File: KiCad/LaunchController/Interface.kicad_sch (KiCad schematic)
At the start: 157 parts

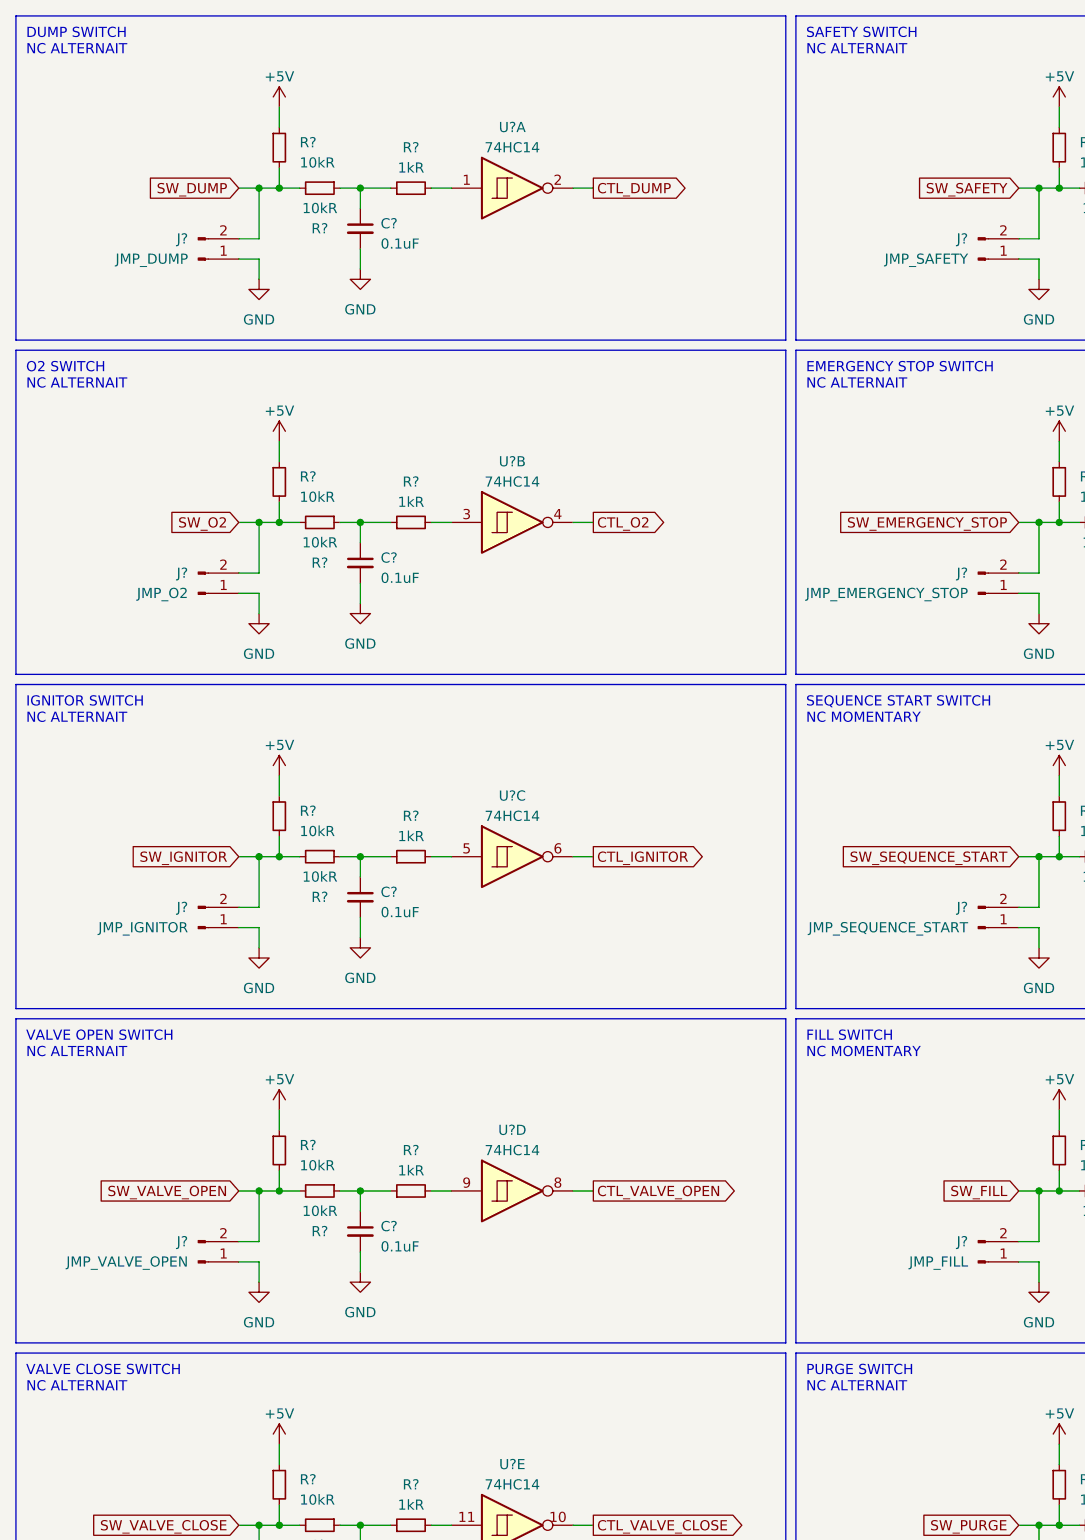
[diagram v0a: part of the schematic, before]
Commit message: スイッチの接点方式を修正
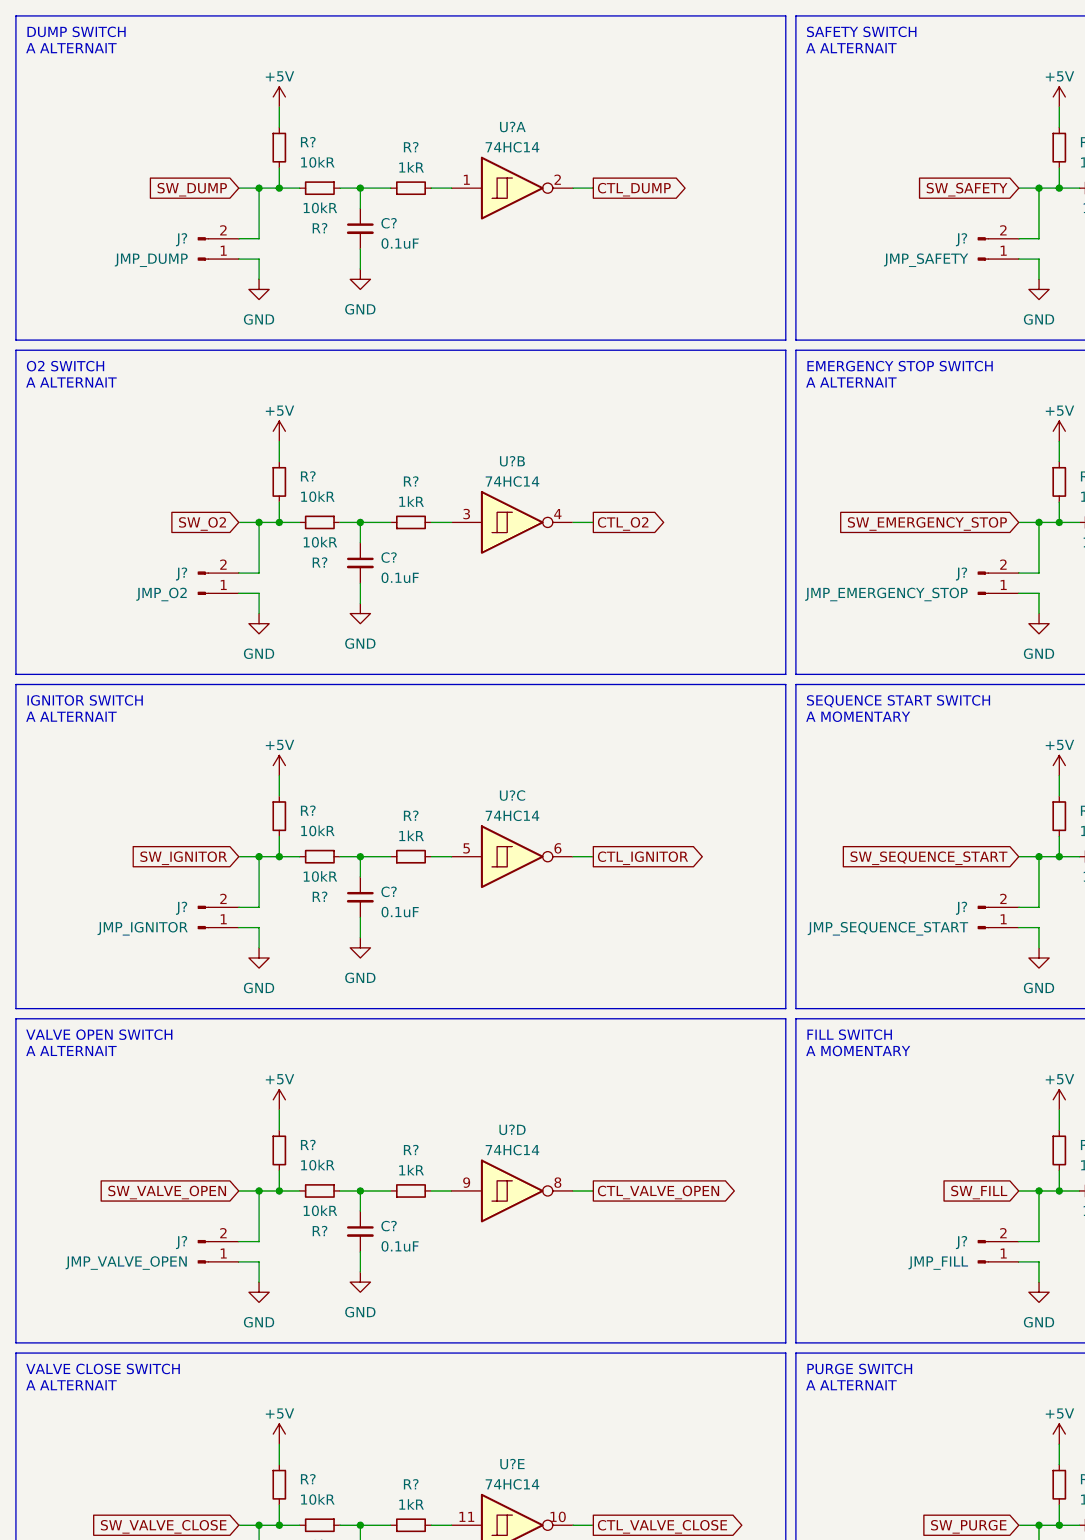
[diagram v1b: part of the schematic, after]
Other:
- note added: "DUMP SWITCH A ALTERNAIT"
- note added: "EMERGENCY STOP SWITCH A ALTERNAIT"
- note added: "FILL SWITCH A MOMENTARY"
- note added: "IGNITOR SWITCH A ALTERNAIT"
- note added: "O2 SWITCH A ALTERNAIT"
- note added: "PURGE SWITCH A ALTERNAIT"
- note added: "SAFETY SWITCH A ALTERNAIT"
- note added: "SEQUENCE START SWITCH A MOMENTARY"
- note added: "VALVE CLOSE SWITCH A ALTERNAIT"
- note added: "VALVE OPEN SWITCH A ALTERNAIT"
- note removed: "DUMP SWITCH NC ALTERNAIT"
- note removed: "EMERGENCY STOP SWITCH NC ALTERNAIT"
- note removed: "FILL SWITCH NC MOMENTARY"
- note removed: "IGNITOR SWITCH NC ALTERNAIT"
- note removed: "O2 SWITCH NC ALTERNAIT"
- note removed: "PURGE SWITCH NC ALTERNAIT"
- note removed: "SAFETY SWITCH NC ALTERNAIT"
- note removed: "SEQUENCE START SWITCH NC MOMENTARY"
- note removed: "VALVE CLOSE SWITCH NC ALTERNAIT"
- note removed: "VALVE OPEN SWITCH NC ALTERNAIT"
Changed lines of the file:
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@@
     (effects (font (size 1.27 1.27)) (justify left bottom))
   )
-  (text "FILL SWITCH\nNC MOMENTARY" (at 111.76 143.51 0)
+  (text "FILL SWITCH\nA MOMENTARY" (at 111.76 143.51 0)
     (effects (font (size 1.27 1.27)) (justify left bottom))
   )
-  (text "EMERGENCY STOP SWITCH\nNC ALTERNAIT" (at 111.76 59.69 0)
+  (text "EMERGENCY STOP SWITCH\nA ALTERNAIT" (at 111.76 59.69 0)
     (effects (font (size 1.27 1.27)) (justify left bottom))
   )
@@
     (effects (font (size 1.27 1.27)) (justify left bottom))
   )
-  (text "IGNITOR SWITCH\nNC ALTERNAIT" (at 13.97 101.6 0)
+  (text "IGNITOR SWITCH\nA ALTERNAIT" (at 13.97 101.6 0)
     (effects (font (size 1.27 1.27)) (justify left bottom))
   )
@@
     (effects (font (size 1.27 1.27)) (justify left bottom))
   )
-  (text "SAFETY SWITCH\nNC ALTERNAIT" (at 111.76 17.78 0)
+  (text "SAFETY SWITCH\nA ALTERNAIT" (at 111.76 17.78 0)
     (effects (font (size 1.27 1.27)) (justify left bottom))
   )
@@
     (effects (font (size 1.27 1.27)) (justify left bottom))
   )
-  (text "O2 SWITCH\nNC ALTERNAIT" (at 13.97 59.69 0)
+  (text "O2 SWITCH\nA ALTERNAIT" (at 13.97 59.69 0)
     (effects (font (size 1.27 1.27)) (justify left bottom))
   )
@@
     (effects (font (size 1.27 1.27)) (justify left bottom))
   )
-  (text "VALVE CLOSE SWITCH\nNC ALTERNAIT" (at 13.97 185.42 0)
+  (text "VALVE CLOSE SWITCH\nA ALTERNAIT" (at 13.97 185.42 0)
     (effects (font (size 1.27 1.27)) (justify left bottom))
   )
@@
     (effects (font (size 1.27 1.27)) (justify left bottom))
   )
-  (text "PURGE SWITCH\nNC ALTERNAIT" (at 111.76 185.42 0)
+  (text "PURGE SWITCH\nA ALTERNAIT" (at 111.76 185.42 0)
     (effects (font (size 1.27 1.27)) (justify left bottom))
   )
-  (text "SEQUENCE START SWITCH\nNC MOMENTARY" (at 111.76 101.6 0)
+  (text "SEQUENCE START SWITCH\nA MOMENTARY" (at 111.76 101.6 0)
     (effects (font (size 1.27 1.27)) (justify left bottom))
   )
-  (text "DUMP SWITCH\nNC ALTERNAIT" (at 13.97 17.78 0)
+  (text "DUMP SWITCH\nA ALTERNAIT" (at 13.97 17.78 0)
     (effects (font (size 1.27 1.27)) (justify left bottom))
   )
-  (text "VALVE OPEN SWITCH\nNC ALTERNAIT" (at 13.97 143.51 0)
+  (text "VALVE OPEN SWITCH\nA ALTERNAIT" (at 13.97 143.51 0)
     (effects (font (size 1.27 1.27)) (justify left bottom))
   )

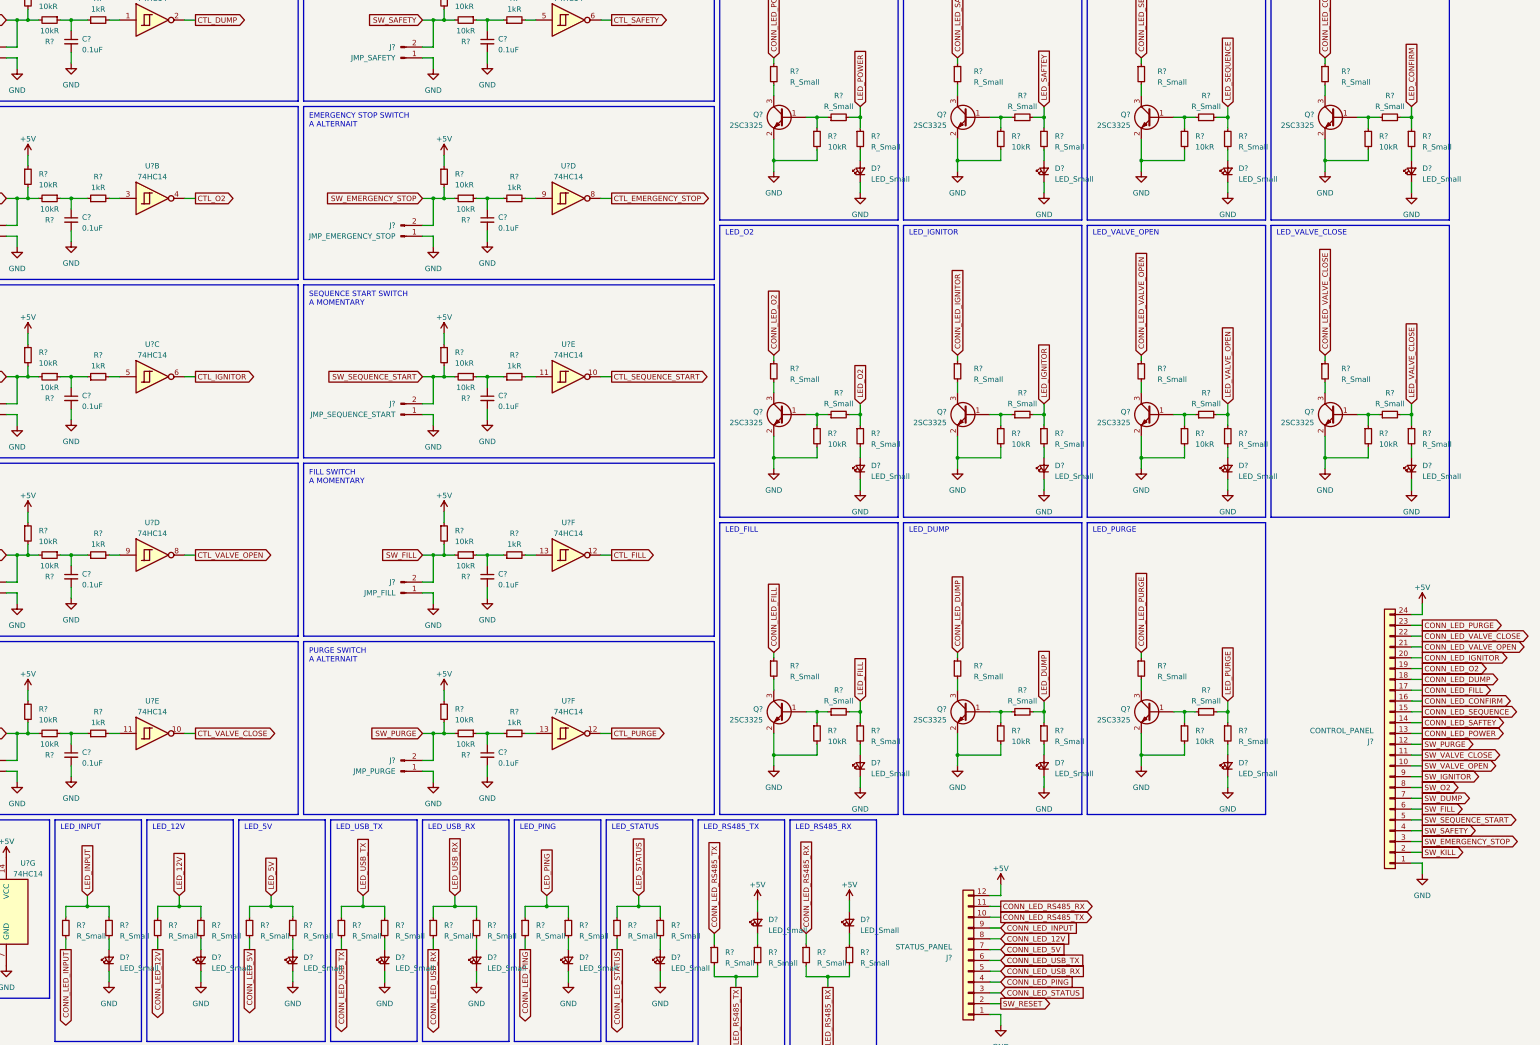
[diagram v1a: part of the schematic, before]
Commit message: LED用の抵抗値を設定
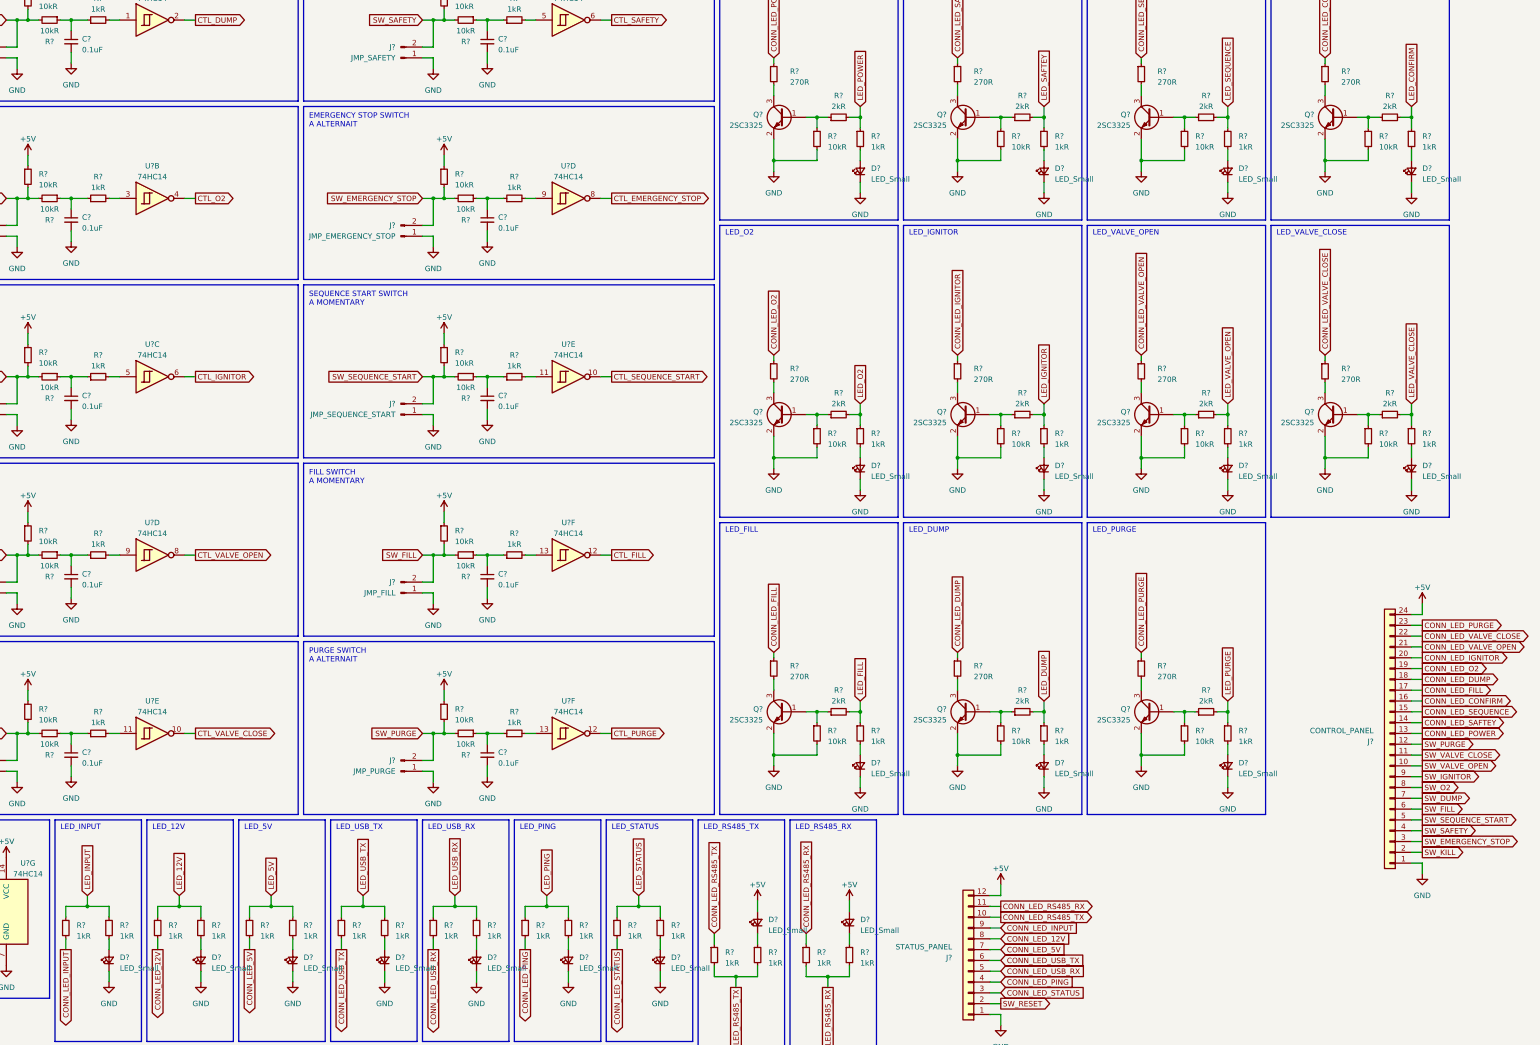
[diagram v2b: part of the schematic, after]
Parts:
- R? (x11): value R_Small -> 270R
- R? (x29): value R_Small -> 1kR
- R? (x11): value R_Small -> 2kR

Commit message: 一通り部品を選定
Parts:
- removed J?: CONTROL_PANEL, symbol Connector_Generic:Conn_01x24
- added J?: INDICATOR_PANEL, Connector_JST:JST_XH_B12B-XH-A_1x12_P2.50mm_Vertical, symbol Connector_Generic:Conn_01x12
- added J?: CONTROL_PANEL, Connector_JST:JST_XH_B12B-XH-A_1x12_P2.50mm_Vertical, symbol Connector_Generic:Conn_01x12
- C? (x10): footprint (none) -> Capacitor_SMD:C_0603_1608Metric_Pad1.08x0.95mm_HandSolder
- D? (x20): value LED_Small -> LED; footprint (none) -> LED_SMD:LED_0603_1608Metric_Pad1.05x0.95mm_HandSolder
- J? (x10): footprint (none) -> Connector_PinHeader_2.54mm:PinHeader_1x02_P2.54mm_Vertical
- J?: footprint (none) -> Connector_JST:JST_XH_B12B-XH-A_1x12_P2.50mm_Vertical
- Q? (x11): value 2SC3325 -> 2SC3325-Y; footprint (none) -> Package_TO_SOT_SMD:SC-59_Handsoldering
- R? (x92): footprint (none) -> Resistor_SMD:R_0603_1608Metric_Pad0.98x0.95mm_HandSolder
- U? (x12): value 74HC14 -> U74HC14; footprint (none) -> Package_DIP:DIP-14_W7.62mm
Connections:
- net +5V: now also J?.12 (Pin_12)
- net CONN_LED_CONFIRM: now also J?.4 (Pin_4)
- net CONN_LED_DUMP: now also J?.6 (Pin_6)
- net CONN_LED_FILL: now also J?.5 (Pin_5)
- net CONN_LED_IGNITOR: now also J?.8 (Pin_8)
- net CONN_LED_O2: now also J?.7 (Pin_7)
- net CONN_LED_POWER: now also J?.1 (Pin_1)
- net CONN_LED_PURGE: now also J?.11 (Pin_11)
- net CONN_LED_SAFTEY: now also J?.2 (Pin_2)
- net CONN_LED_SEQUENCE: now also J?.3 (Pin_3)
- net CONN_LED_VALVE_CLOSE: now also J?.10 (Pin_10)
- net CONN_LED_VALVE_OPEN: now also J?.9 (Pin_9)
- net GND: now also J?.1 (Pin_1)
- net SW_DUMP: now also J?.7 (Pin_7)
- net SW_EMERGENCY_STOP: now also J?.3 (Pin_3)
- net SW_FILL: now also J?.6 (Pin_6)
- net SW_IGNITOR: now also J?.9 (Pin_9)
- net SW_KILL: now also J?.2 (Pin_2)
- net SW_O2: now also J?.8 (Pin_8)
- net SW_PURGE: now also J?.12 (Pin_12)
- net SW_SAFETY: now also J?.4 (Pin_4)
- net SW_SEQUENCE_START: now also J?.5 (Pin_5)
- net SW_VALVE_CLOSE: now also J?.11 (Pin_11)
- net SW_VALVE_OPEN: now also J?.10 (Pin_10)
